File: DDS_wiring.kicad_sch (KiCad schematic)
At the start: 12 parts, among them J1 Raspberry_Pi_2_3, U1 XPT2046TS, U2 MPU-6050, U3 MPU-6050, U4 MPU-6050, U5 ADS1015IDGS, U6 ADS1015IDGS, U7 RS485

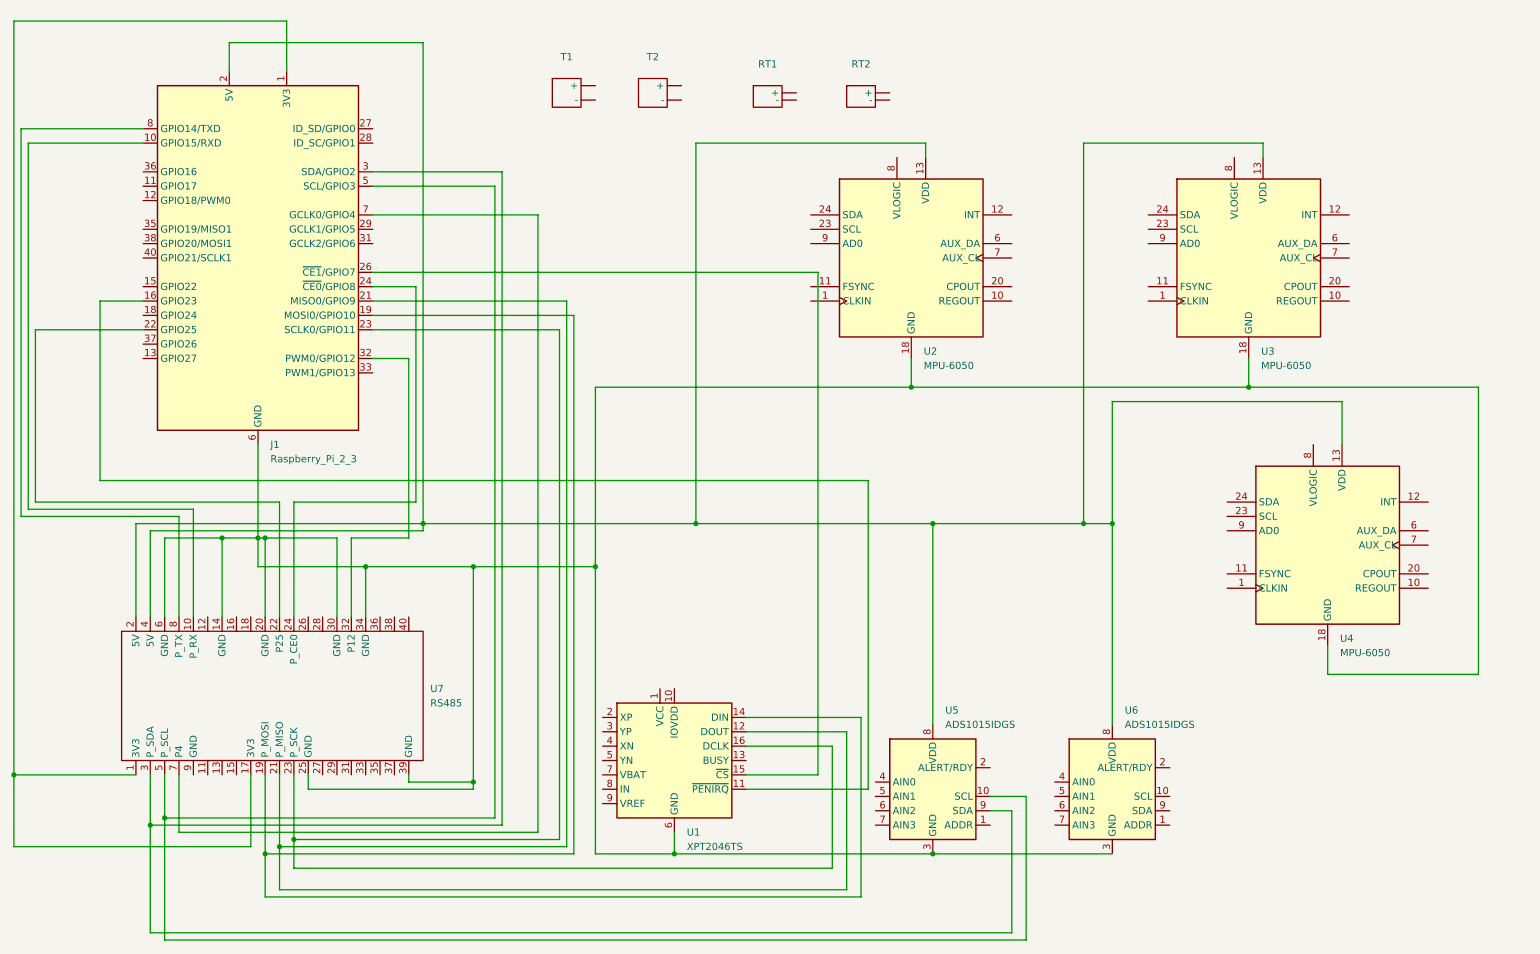
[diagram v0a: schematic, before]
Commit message: Connected NTC & M3200s + Addressing
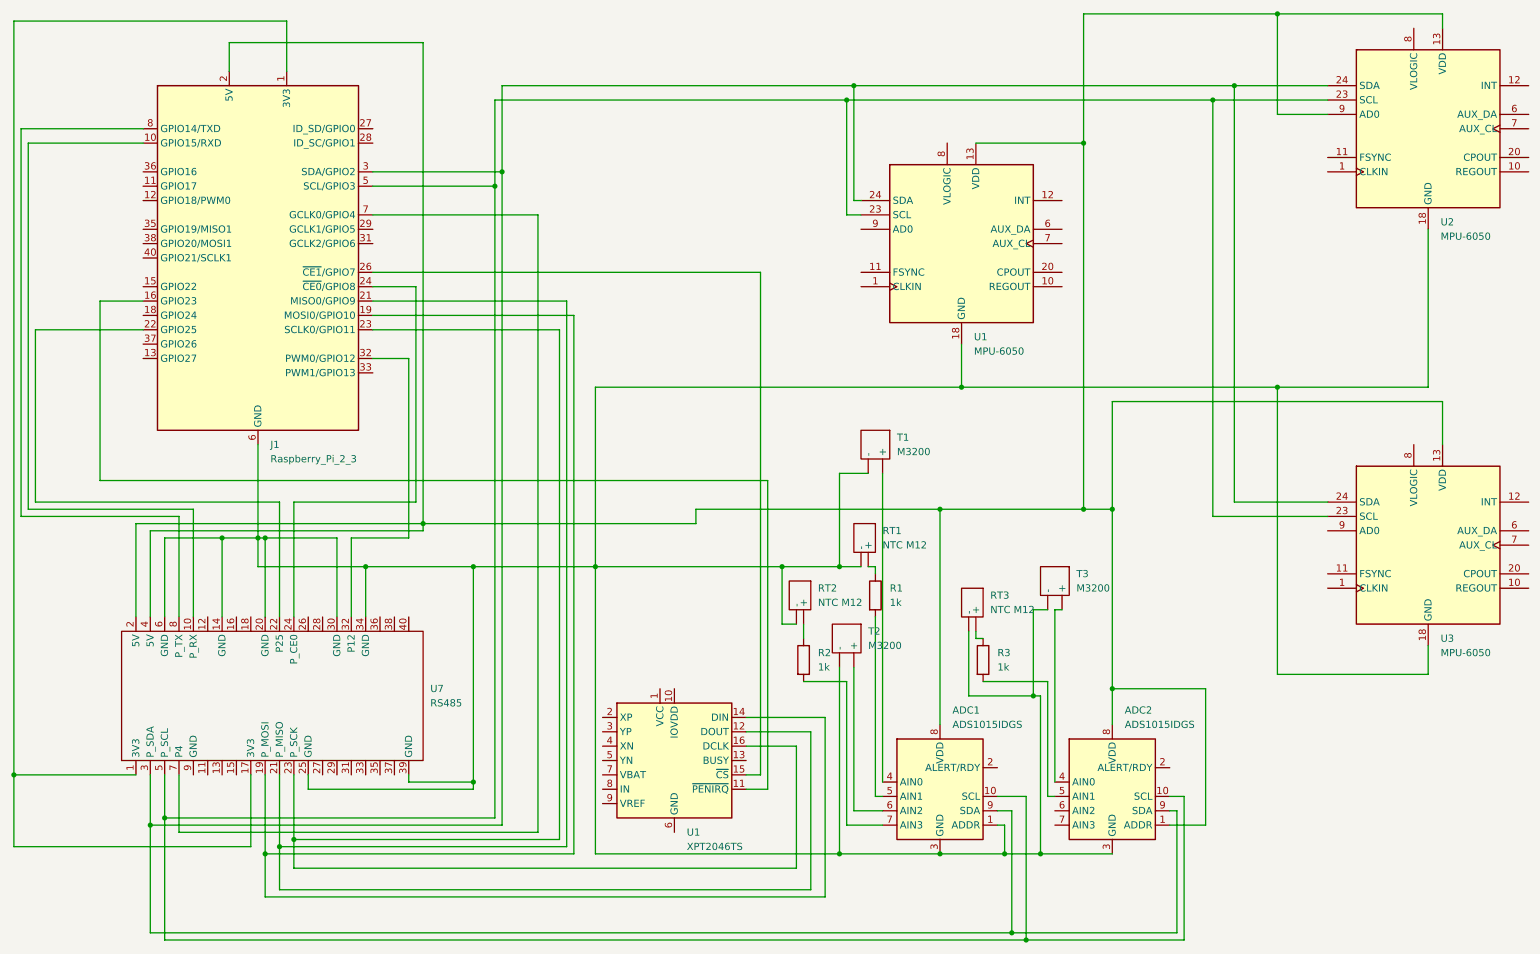
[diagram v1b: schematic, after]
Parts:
- added R1, R2, R3: 1k, symbol Device:R
- added RT3: NTC M12, symbol BUTM_JC:NTC_M12
- added T3: M3200, symbol BUTM_JC:M3200
- RT1, RT2: value ~ -> NTC M12
- T1, T2: value ~ -> M3200
- renumbered U5 to ADC1, U6 to ADC2, U2 to U1, U3 to U2, U4 to U3
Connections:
- net at RT2. (-): now also R2.1
- net at ADC1.3 (GND), ADC2.3 (GND), J1.14 (GND)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: now also ADC1.1 (ADDR), RT1. (-), RT2. (-), T1. (-), T2. (-), RT3. (-), T3. (-); no longer U1.6 (GND)
- net at ADC1.8 (VDD), ADC2.8 (VDD), J1.2 (5V)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: now also ADC2.1 (ADDR), U2.9 (AD0)
- net at ADC1.9 (SDA), J1.3 (SDA/GPIO2), U7.3 (P_SDA): now also ADC2.9 (SDA), U1.24 (SDA), U2.24 (SDA), U3.24 (SDA)
- net at ADC1.10 (SCL), J1.5 (SCL/GPIO3), U7.5 (P_SCL): now also ADC2.10 (SCL), U1.23 (SCL), U2.23 (SCL), U3.23 (SCL)
- net at RT1. (-): now also R1.1
- net at ADC2.4 (AIN0): now also T3. (-)
- net at ADC2.5 (AIN1): now also R3.2
- net at T1. (-): now also ADC1.4 (AIN0)
- net at ADC1.5 (AIN1): now also R1.2
- net at ADC1.6 (AIN2): now also T2. (-)
- net at ADC1.7 (AIN3): now also R2.2
- new net: R3.1, RT3. (-)
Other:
- moved on the sheet: ADC1, RT1, RT2, T1, T2, U1, U2, U3
